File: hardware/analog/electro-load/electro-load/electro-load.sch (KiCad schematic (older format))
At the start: 28 parts, among them J1 AVR-ISP-10, SW1 RESET, U1 ATmega328P-AU, U10 ADS1115IDGS, U11 ADS1115IDGS, U2 MCP4725A0T-E_CH, U8 REF5040ID, U9 LMV321

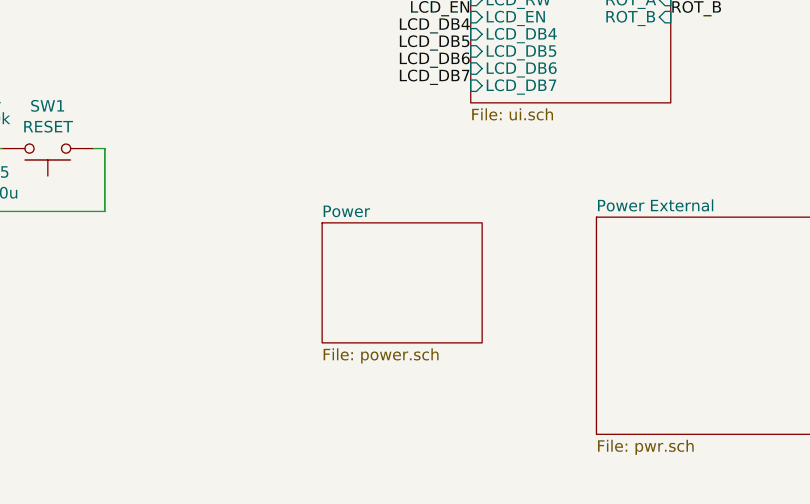
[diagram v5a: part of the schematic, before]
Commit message: Added basic 3D model of amplifier encasing
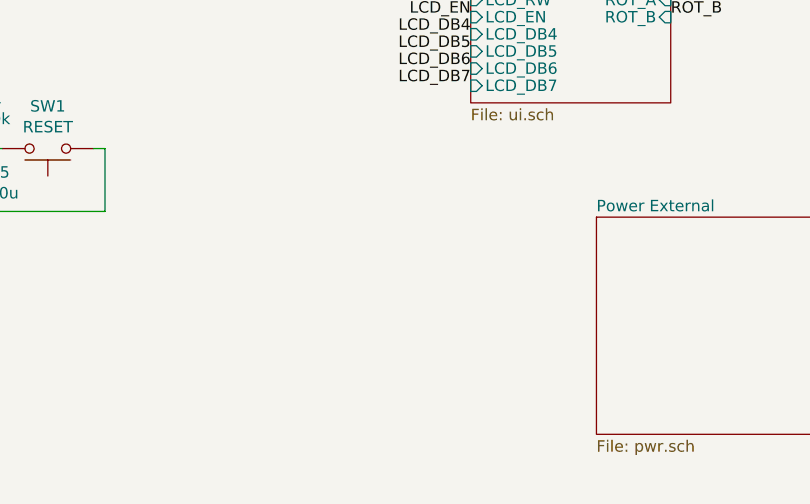
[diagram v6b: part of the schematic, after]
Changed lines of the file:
@@
 EESchema Schematic File Version 4
-LIBS:electro-load-cache
 EELAYER 30 0
 EELAYER END
 $Descr A4 11693 8268
 encoding utf-8
-Sheet 1 6
+Sheet 1 5
 Title ""
 Date ""
@@
 	3975 1150 3975 1250
 Connection ~ 3975 1250
-$Sheet
-S 4650 6100 700  525
-U 5E8D69C1
-F0 "Power" 50
-F1 "power.sch" 50
-$EndSheet
 Text Label 2600 6275 0    50   ~ 0
 LCD_RS

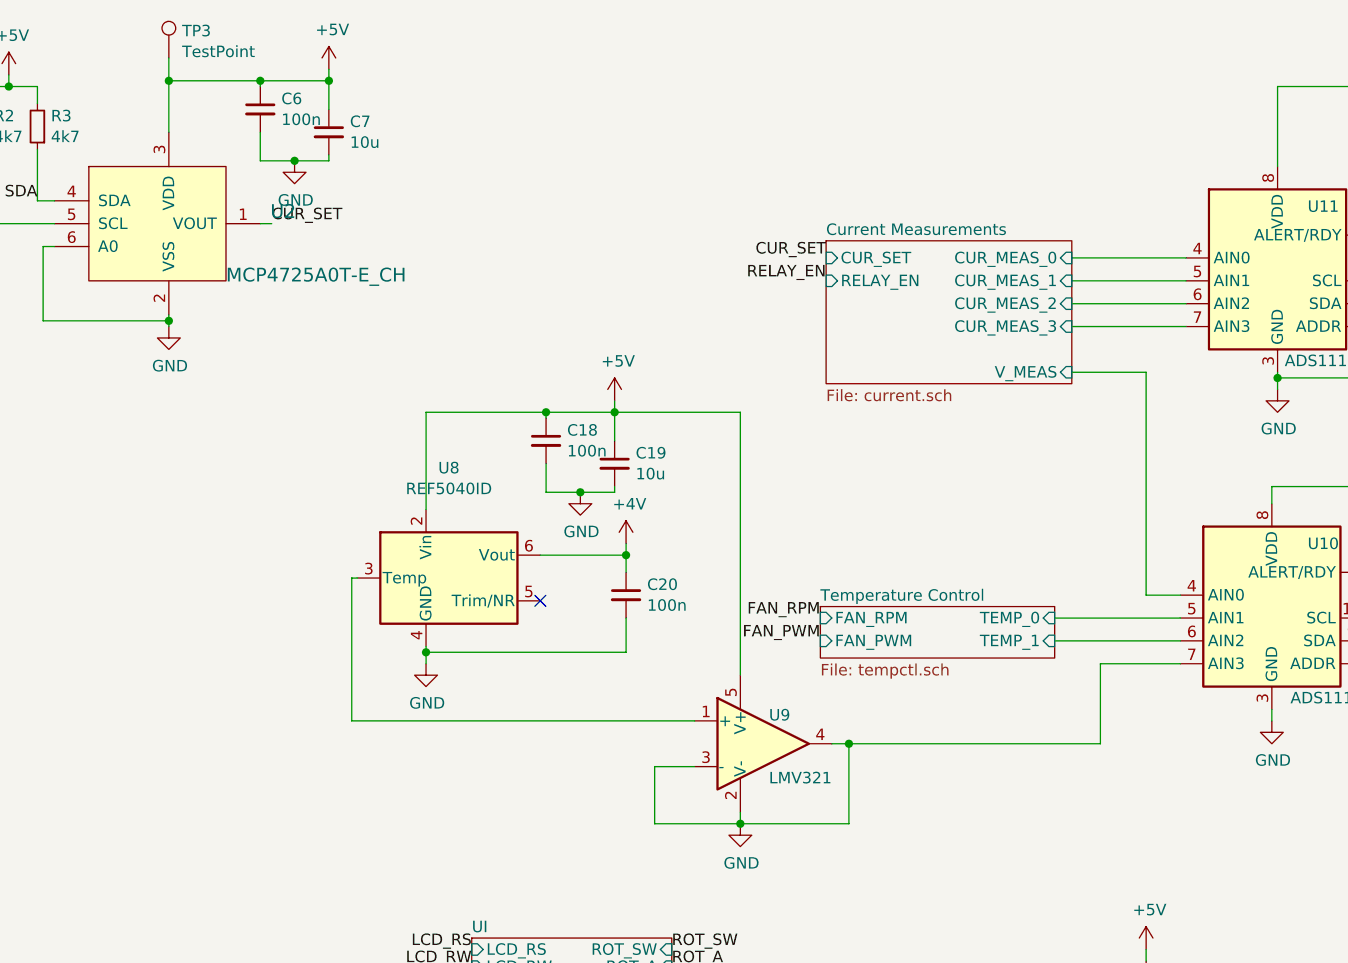
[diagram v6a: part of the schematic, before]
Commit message: Changed pin connections to/from lmv324 in order to avoid bird nesting. Widened traces for 5V and LOAD_CURRENT. Added four power resistors to the fab layer. Arranged left side analogs
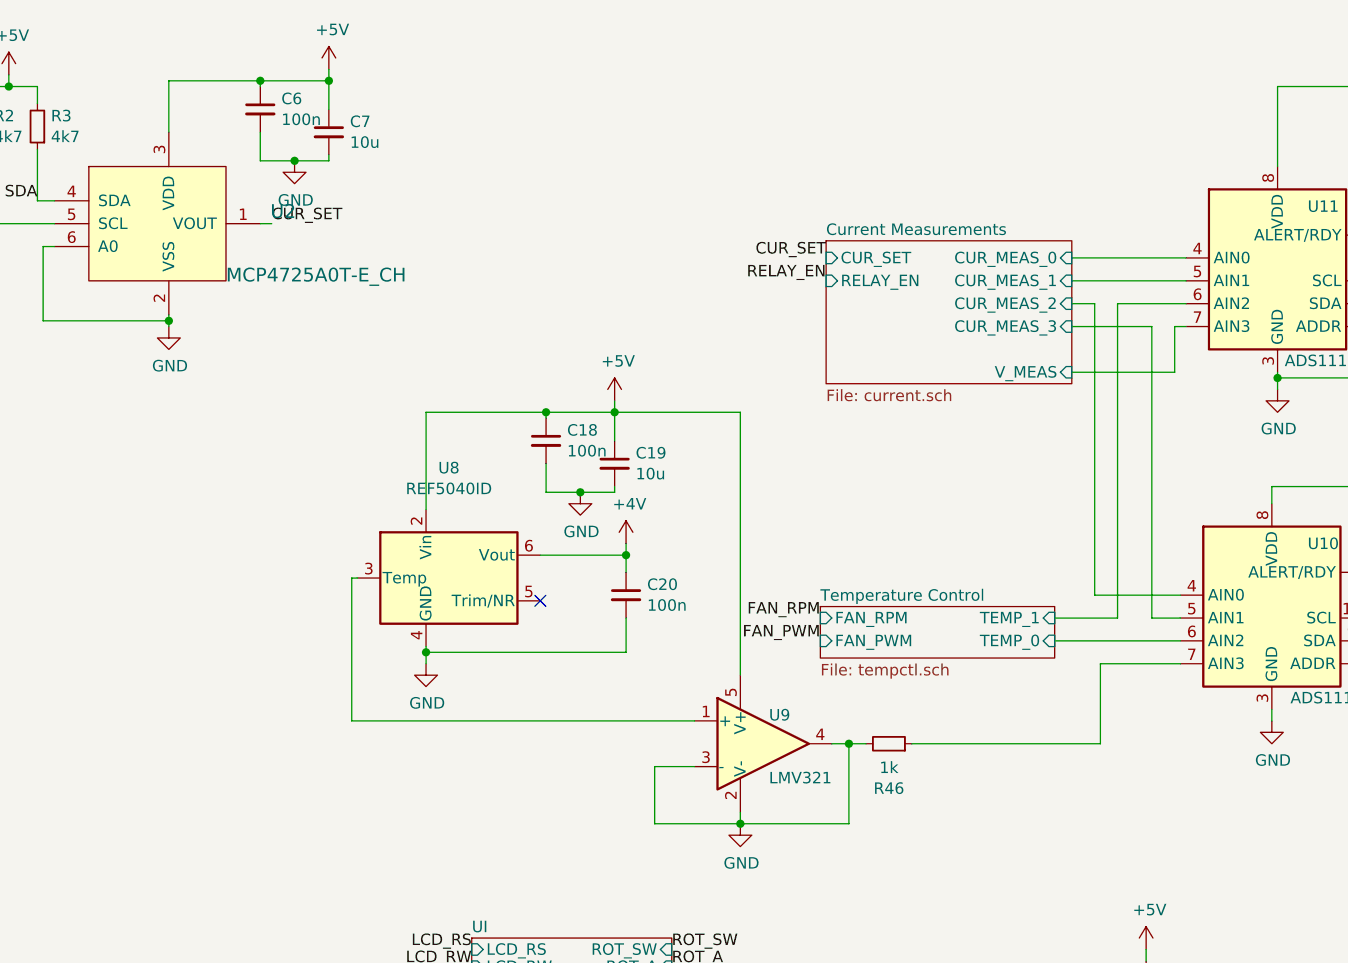
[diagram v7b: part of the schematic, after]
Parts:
- removed TP3: TestPoint, athir:testpoint_probe, symbol Connector:TestPoint
- added R46: 1k, Resistor_SMD:R_0603_1608Metric, symbol Device:R_Small
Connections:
- net Current Measurements/CUR_MEAS_2: now also U10.4 (AIN0); no longer U11.6 (AIN2)
- net Current Measurements/CUR_MEAS_3: now also U10.5 (AIN1); no longer U11.7 (AIN3)
- net Current Measurements/V_MEAS: now also U11.7 (AIN3); no longer U10.4 (AIN0)
- net GND: now also R46.2; no longer U10.7 (AIN3)
- net Temperature Control/TEMP_0: now also U10.6 (AIN2); no longer U10.5 (AIN1)
- net Temperature Control/TEMP_1: now also U11.6 (AIN2); no longer U10.6 (AIN2)
- new net: R46.1, U10.7 (AIN3)
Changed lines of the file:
@@
 Wire Wire Line
 	1100 4150 1100 4275
-$Comp
-L Connector:TestPoint TP3
-U 1 1 5E9DB920
-P 3975 1150
-F 0 "TP3" H 4033 1268 50  0000 L CNN
-F 1 "TestPoint" H 4033 1177 50  0000 L CNN
-F 2 "athir:testpoint_probe" H 4175 1150 50  0001 C CNN
-F 3 "~" H 4175 1150 50  0001 C CNN
-	1    3975 1150
-	1    0    0    -1
-$EndComp
-Wire Wire Line
-	3975 1150 3975 1250
-Connection ~ 3975 1250
 Text Label 2600 6275 0    50   ~ 0
 LCD_RS
@@
 F0 "Temperature Control" 50
 F1 "tempctl.sch" 50
-F2 "TEMP_1" I R 7850 3700 50
-F3 "TEMP_0" I R 7850 3600 50
+F2 "TEMP_1" I R 7850 3600 50
+F3 "TEMP_0" I R 7850 3700 50
 F4 "FAN_RPM" I L 6825 3600 50
 F5 "FAN_PWM" I L 6825 3700 50
@@
 Wire Wire Line
 	8425 2125 7925 2125
-Wire Wire Line
-	7925 2225 8425 2225
-Wire Wire Line
-	8425 2325 7925 2325
 $Comp
 L power:GND #PWR063
@@
 	8800 4050 8800 4000
 Wire Wire Line
-	7925 2525 8250 2525
-Wire Wire Line
-	8250 2525 8250 3500
-Wire Wire Line
-	8250 3500 8400 3500
-Wire Wire Line
-	8400 3600 7850 3600
-Wire Wire Line
-	7850 3700 8400 3700
+	7925 2525 8375 2525
 $Comp
 L Device:C_Small C21
@@
 	8050 3800 8050 4150
 Wire Wire Line
-	8050 4150 6950 4150
-Wire Wire Line
 	6275 4050 4775 4050
 Wire Wire Line
@@
 Wire Wire Line
 	6475 4500 6950 4500
-Connection ~ 6950 4150
 Wire Wire Line
 	6950 4150 6875 4150
@@
 F1 "pwr.sch" 50
 $EndSheet
+$Comp
+L Device:R_Small R46
+U 1 1 5EAF425B
+P 7125 4150
+AR Path="/5EAF425B" Ref="R46"  Part="1"
+AR Path="/5E789C0B/5EAF425B" Ref="R?"  Part="1"
+F 0 "R46" V 6929 4150 50  0000 C CNN
+F 1 "1k" V 7020 4150 50  0000 C CNN
+F 2 "Resistor_SMD:R_0603_1608Metric" H 7125 4150 50  0001 C CNN
+F 3 "~" H 7125 4150 50  0001 C CNN
+	1    7125 4150
+	0    1    -1   0
+$EndComp
+Wire Wire Line
+	7025 4150 6950 4150
+Connection ~ 6950 4150
+Wire Wire Line
+	7225 4150 8050 4150
+Wire Wire Line
+	8125 2225 8425 2225
+Wire Wire Line
+	7925 2225 8025 2225
+Wire Wire Line
+	8375 2525 8375 2325
+Wire Wire Line
+	8375 2325 8425 2325
+Wire Wire Line
+	8025 2225 8025 3500
+Wire Wire Line
+	8025 3500 8400 3500
+Wire Wire Line
+	8400 3600 8275 3600
+Wire Wire Line
+	8275 3600 8275 2325
+Wire Wire Line
+	8275 2325 7925 2325
+Wire Wire Line
+	8125 2225 8125 3600
+Wire Wire Line
+	8125 3600 7850 3600
+Wire Wire Line
+	7850 3700 8400 3700
 $EndSCHEMATC

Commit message: All traces layed out. Silkscreen and finishing touches needed.
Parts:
- added TP3, TP8: TestPoint, athir:testpoint_probe, symbol Connector:TestPoint
- SW1: footprint (none) -> Button_Switch_THT:SW_PUSH_6mm_H4.3mm; symbol Switch:SW_Push -> Switch:SW_SPST
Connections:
- net +4V: now also TP3.1
- net +5V: no longer TP1.1
- net GND: now also SW1.2 (B), TP1.1; no longer R46.2, SW1.1, U9.3 (-), U9.4
- net ~RESET: now also SW1.1 (A); no longer SW1.2
- net at R46.1, U10.7 (AIN3): now also TP8.1
- new net: R46.2, U9.3 (-), U9.4
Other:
- moved on the sheet: TP1
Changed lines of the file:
@@
 	3100 6075 3100 6050
 $Comp
-L Switch:SW_Push SW1
+L Switch:SW_SPST SW1
 U 1 1 5E87E97B
 P 3450 5775
 F 0 "SW1" H 3450 5590 50  0000 C CNN
 F 1 "RESET" H 3450 5681 50  0000 C CNN
-F 2 "" H 3450 5975 50  0001 C CNN
+F 2 "Button_Switch_THT:SW_PUSH_6mm_H4.3mm" H 3450 5975 50  0001 C CNN
 F 3 "~" H 3450 5975 50  0001 C CNN
 	1    3450 5775
-	-1   0    0    1
+	1    0    0    -1
 $EndComp
 Wire Wire Line
@@
 L Connector:TestPoint TP1
 U 1 1 5E9A7122
-P 1100 4150
-F 0 "TP1" H 1158 4268 50  0000 L CNN
-F 1 "TestPoint" H 1158 4177 50  0000 L CNN
-F 2 "athir:testpoint_probe" H 1300 4150 50  0001 C CNN
-F 3 "~" H 1300 4150 50  0001 C CNN
-	1    1100 4150
-	1    0    0    -1
-$EndComp
-Wire Wire Line
-	1100 4150 1100 4275
+P 1050 3775
+F 0 "TP1" H 1108 3893 50  0000 L CNN
+F 1 "TestPoint" H 1108 3802 50  0000 L CNN
+F 2 "athir:testpoint_probe" H 1250 3775 50  0001 C CNN
+F 3 "~" H 1250 3775 50  0001 C CNN
+	1    1050 3775
+	1    0    0    -1
+$EndComp
 Text Label 2600 6275 0    50   ~ 0
 LCD_RS
@@
 $EndComp
 Wire Wire Line
-	5975 3400 5975 3325
+	5975 3400 5975 3350
 Connection ~ 5975 3325
 Wire Wire Line
@@
 L power:GND #PWR061
 U 1 1 5E9FF60A
-P 6475 4500
-F 0 "#PWR061" H 6475 4250 50  0001 C CNN
-F 1 "GND" H 6480 4327 50  0000 C CNN
-F 2 "" H 6475 4500 50  0001 C CNN
-F 3 "" H 6475 4500 50  0001 C CNN
-	1    6475 4500
-	1    0    0    -1
-$EndComp
-Wire Wire Line
-	6475 4500 6475 4450
+P 6475 4600
+F 0 "#PWR061" H 6475 4350 50  0001 C CNN
+F 1 "GND" H 6480 4427 50  0000 C CNN
+F 2 "" H 6475 4600 50  0001 C CNN
+F 3 "" H 6475 4600 50  0001 C CNN
+	1    6475 4600
+	1    0    0    -1
+$EndComp
 Wire Wire Line
 	6275 4250 6100 4250
@@
 	6100 4250 6100 4500
 Wire Wire Line
-	6100 4500 6475 4500
-Wire Wire Line
 	6950 4500 6950 4150
-Connection ~ 6475 4500
-Wire Wire Line
-	6475 4500 6950 4500
 Wire Wire Line
 	6950 4150 6875 4150
@@
 Connection ~ 6950 4150
 Wire Wire Line
-	7225 4150 8050 4150
+	7225 4150 7400 4150
 Wire Wire Line
 	8125 2225 8425 2225
@@
 Wire Wire Line
 	7850 3700 8400 3700
+Wire Wire Line
+	6100 4500 6950 4500
+Wire Wire Line
+	6475 4450 6475 4600
+$Comp
+L Connector:TestPoint TP3
+U 1 1 5EC5D453
+P 6150 3325
+F 0 "TP3" H 6208 3443 50  0000 L CNN
+F 1 "TestPoint" H 6208 3352 50  0000 L CNN
+F 2 "athir:testpoint_probe" H 6350 3325 50  0001 C CNN
+F 3 "~" H 6350 3325 50  0001 C CNN
+	1    6150 3325
+	1    0    0    -1
+$EndComp
+Wire Wire Line
+	6150 3325 6150 3350
+Wire Wire Line
+	6150 3350 5975 3350
+Connection ~ 5975 3350
+Wire Wire Line
+	5975 3350 5975 3325
+$Comp
+L Connector:TestPoint TP8
+U 1 1 5EC63BF8
+P 7400 4075
+F 0 "TP8" H 7458 4193 50  0000 L CNN
+F 1 "TestPoint" H 7458 4102 50  0000 L CNN
+F 2 "athir:testpoint_probe" H 7600 4075 50  0001 C CNN
+F 3 "~" H 7600 4075 50  0001 C CNN
+	1    7400 4075
+	1    0    0    -1
+$EndComp
+Wire Wire Line
+	7400 4075 7400 4150
+Connection ~ 7400 4150
+Wire Wire Line
+	7400 4150 8050 4150
+$Comp
+L power:GND #PWR0107
+U 1 1 5EC872D1
+P 1050 3875
+F 0 "#PWR0107" H 1050 3625 50  0001 C CNN
+F 1 "GND" H 1055 3702 50  0000 C CNN
+F 2 "" H 1050 3875 50  0001 C CNN
+F 3 "" H 1050 3875 50  0001 C CNN
+	1    1050 3875
+	1    0    0    -1
+$EndComp
+Wire Wire Line
+	1050 3875 1050 3775
 $EndSCHEMATC
